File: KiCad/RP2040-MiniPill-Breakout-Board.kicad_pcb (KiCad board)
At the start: 2 copper layers, 52 x 66.5 mm, 17 parts, among them J1 Conn_01x20_Socket, J2 Conn_01x20_Socket, J3 Screw_Terminal_01x20, J4 Screw_Terminal_01x20, U1 TPS3700

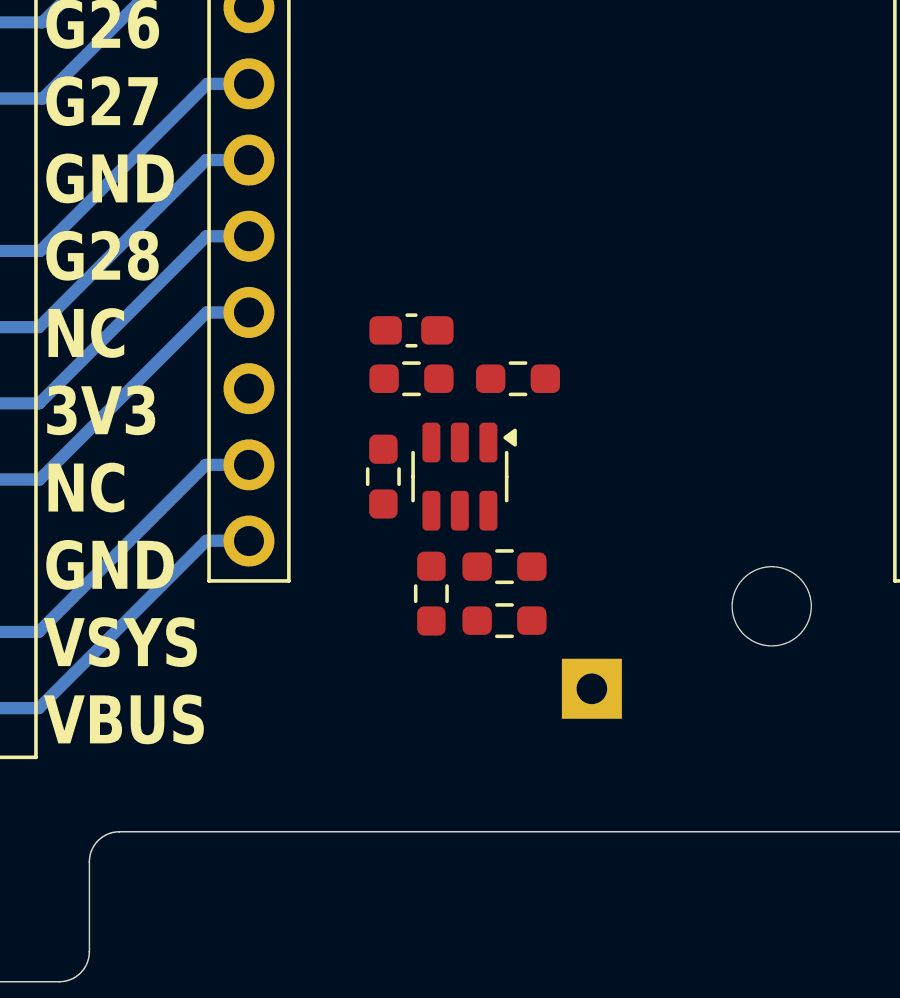
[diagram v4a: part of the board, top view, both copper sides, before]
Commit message: adding diode and making first placement
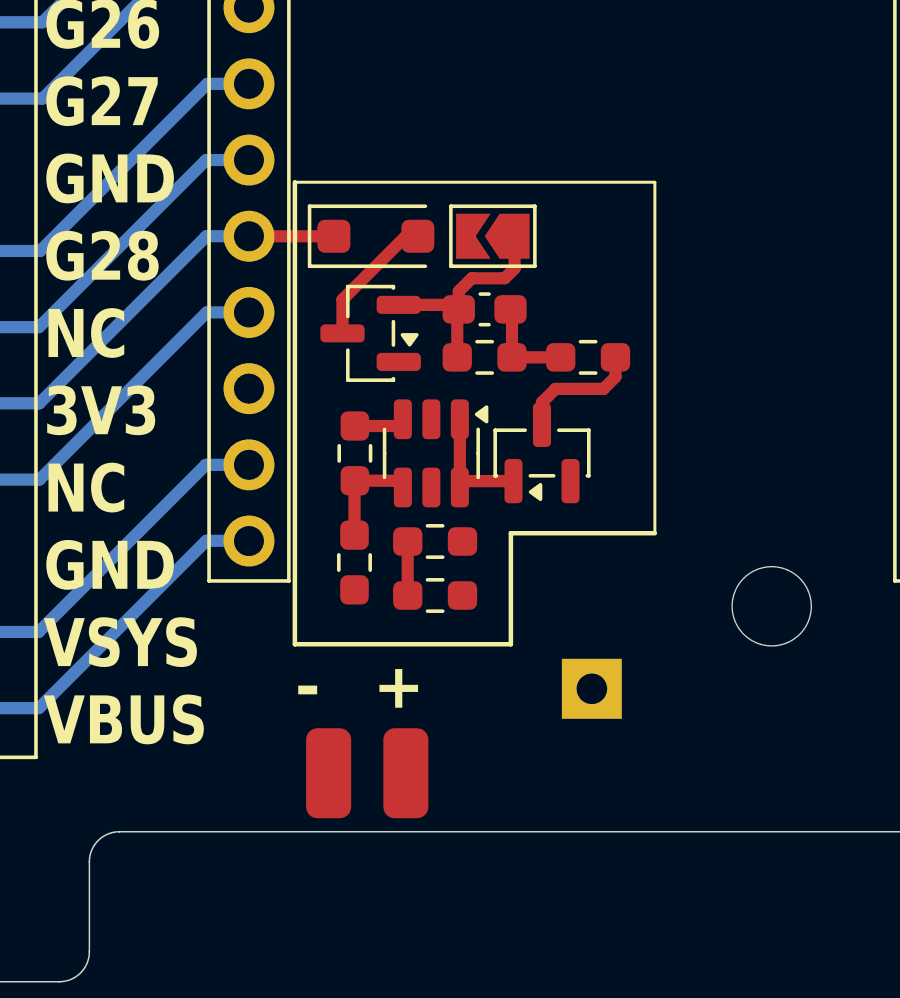
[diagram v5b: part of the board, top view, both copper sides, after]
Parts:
- added D1: MBR120VLSFT1G, Diode_SMD:D_SOD-123F, F.Cu at (137.0, 103.1)
- added GND: SolderWirePad_1x01_SMD_1.5x3mm, Connector_Wire:SolderWirePad_1x01_SMD_1.5x3mm, F.Cu at (135.4, 121.0)
- added JP1: SolderJumper_2_Open, Jumper:SolderJumper-2_P1.3mm_Open_TrianglePad1.0x1.5mm, F.Cu at (140.9, 103.1)
- added Q1: IRLML6402, Package_TO_SOT_SMD:SOT-23, F.Cu at (136.8, 106.3)
- added Q2: IRLML2502, Package_TO_SOT_SMD:SOT-23, F.Cu at (142.5, 110.3)
- added VDD: SolderWirePad_1x01_SMD_1.5x3mm, Connector_Wire:SolderWirePad_1x01_SMD_1.5x3mm, F.Cu at (138.0, 121.0)
- moved R3 2.76 mm to (136.3, 114.0)
- moved R5 2.54 mm to (140.6, 107.1)
- moved C1 2.54 mm to (140.6, 105.5)
- moved R1 2.46 mm to (139.0, 115.1)
- moved R4 2.46 mm to (139.0, 113.3)
- moved R6 2.44 mm to (144.1, 107.1)
- moved U1 1.23 mm to (138.8, 110.3)
- moved R2 1.23 mm to (136.3, 110.3)
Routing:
- net /VDD: track 0.00 -> 9.37 mm
- net Net-(D1-A): track 0.00 -> 4.51 mm
- net Net-(Q2-D): track 0.00 -> 4.20 mm
- net Net-(Q2-G): track 0.00 -> 4.15 mm
- net Net-(U1-INB): track 0.00 -> 3.51 mm
- net Net-(Q1-G): track 0.00 -> 3.25 mm
- net /3V3: track 12.6 -> 15.5 mm
- net Net-(U1-INA): track 0.00 -> 1.69 mm
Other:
- board text added: "+"
- board text added: "-"

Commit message: adding LCSC Parts
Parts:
- moved R6 1.21 mm to (143.2, 106.3), turned to 90 degrees
- moved R1 0.42 mm to (139.0, 114.7)
- moved GND 0.32 mm to (135.8, 121.0)
- moved JP1 0.25 mm to (141.2, 103.1)
- moved D1 0.20 mm to (137.2, 103.1)
- moved R3 0.18 mm to (136.2, 113.8)
- moved R4 0.18 mm to (139.0, 113.1)
- moved Q2 0.14 mm to (142.6, 110.2)
- moved U1 0.14 mm to (138.8, 110.2)
- moved Q1 0.12 mm to (136.9, 106.3)
- moved R2 0.09 mm to (136.3, 110.2)
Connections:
- J1 pad 15: /NC -> Net-(J1-Pin_15)
- J1 pad 17: /NC -> Net-(J1-Pin_17)
- J3 pad 15: /NC -> Net-(J1-Pin_15)
- J3 pad 17: /NC -> Net-(J1-Pin_17)
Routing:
- net /NC: track 25.3 -> 0.00 mm
- net Net-(J1-Pin_17): track 0.00 -> 12.6 mm
- net Net-(J1-Pin_15): track 0.00 -> 12.6 mm
- net Net-(Q1-G): track 3.25 -> 8.10 mm
- net Net-(D1-A): track 4.51 -> 6.59 mm
- net Net-(Q2-G): track 4.15 -> 6.01 mm
- net Net-(Q2-D): track 4.20 -> 5.60 mm
- net GND: track 0.00 -> 0.99 mm, vias 0 -> 1
- added copper zone on F.Cu, net /VDD
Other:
- board text added: "Over-/Undervoltage monitoring circuit"
- board text added: "RP2040-MiniPill-Breakout-Board"

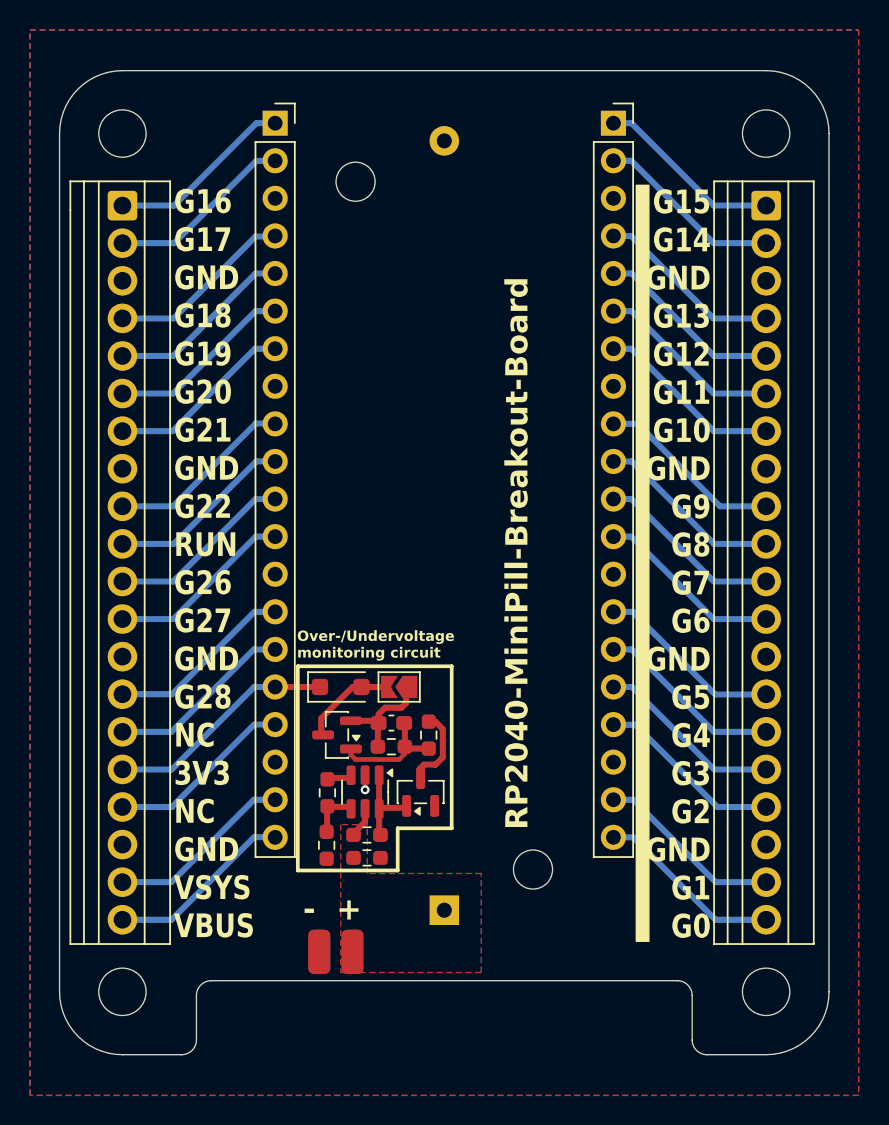
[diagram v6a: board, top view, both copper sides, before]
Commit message: making some finetuning and adding silkscreens, 3dvieports, etc.
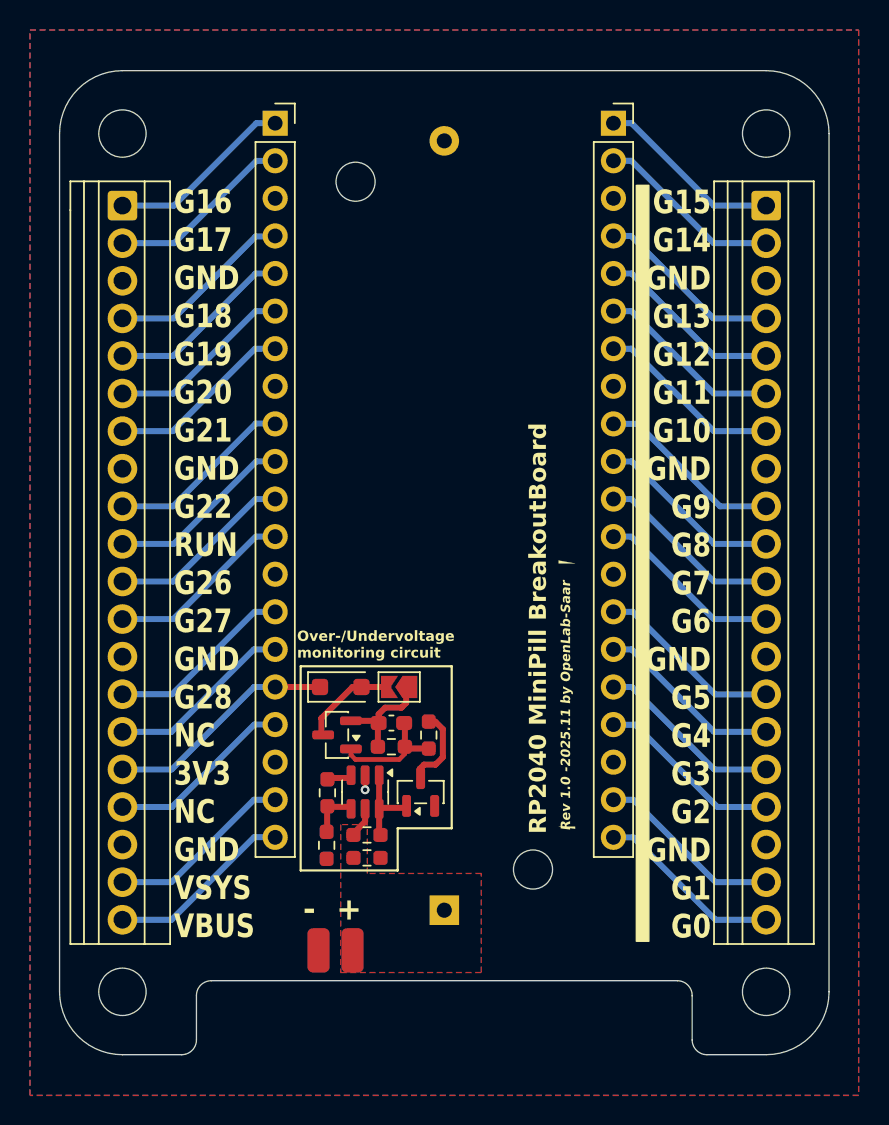
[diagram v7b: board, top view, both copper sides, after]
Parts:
- added REF**: OSHW-Logo2_7.3x6mm_SilkScreen, Symbol:OSHW-Logo2_7.3x6mm_SilkScreen, B.Cu at (127.4, 84.0)
- added REF**: WEEE-Logo_4.2x6mm_SilkScreen, Symbol:WEEE-Logo_4.2x6mm_SilkScreen, B.Cu at (127.8, 78.4)
- added REF**: KiCad-Logo2_5mm_SilkScreen, Symbol:KiCad-Logo2_5mm_SilkScreen, B.Cu at (127.8, 113.1)
- added REF**: ESD-Logo_6.6x6mm_SilkScreen, Symbol:ESD-Logo_6.6x6mm_SilkScreen, B.Cu at (127.8, 72.7)
- moved GND 0.11 mm to (135.7, 120.9)
- moved VDD 0.10 mm to (138.0, 120.9)
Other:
- board text added: "RP2040 MiniPill BreakoutBoard"
- board text added: "Rev 1.0 -2025.11 by OpenLab-Saar"
- board text added: "https://github.com/dokuhn/RP2040-MiniPill-Breakout-Board"
- board text removed: "RP2040-MiniPill-Breakout-Board"

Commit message: making  some finetuning
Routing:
- net /VDD: track 9.60 -> 18.3 mm, vias 0 -> 3
- net Net-(U1-INA): track 1.71 -> 10.2 mm, vias 0 -> 2
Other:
- outline, holes or cut-outs redrawn
